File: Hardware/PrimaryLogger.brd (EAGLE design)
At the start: 52.1 x 77.1 mm, 92 parts, among them J1 CONN_42.54_SCREW, J2 CONN_42.54_SCREW, J3 CONN_42.54_SCREW, J4 CONN_42.54_SCREW, J5 CONN_32.54_SCREW, Q1 DMG3404, Q2 DMG3404, U1 MIC2005, U10 TPL5010DDC, U11 MIC842, U12 PCA9617TSSOP8, U13 MCP23008SSOP, U2 MIC2005, U25 SN74AUP3G34DCU, U3 TPL5010DDC, U4 TXS0102DCU, U5 SN74LVC1G3157SC70, U6 TCS3400, U7 SHTC3DFN, U8 MCP23008QFN, U9 MCP7940SOIC

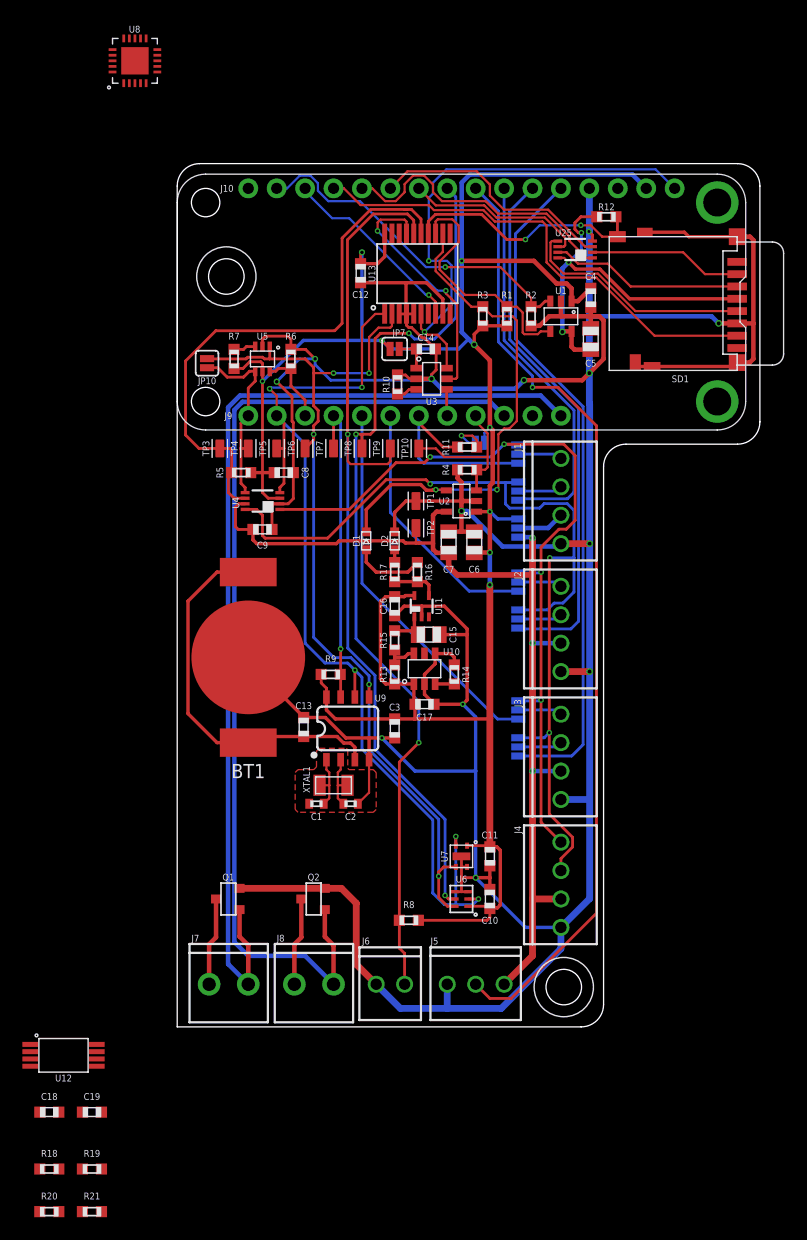
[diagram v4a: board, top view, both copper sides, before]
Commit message: Added Niagara, jumpers, power connector
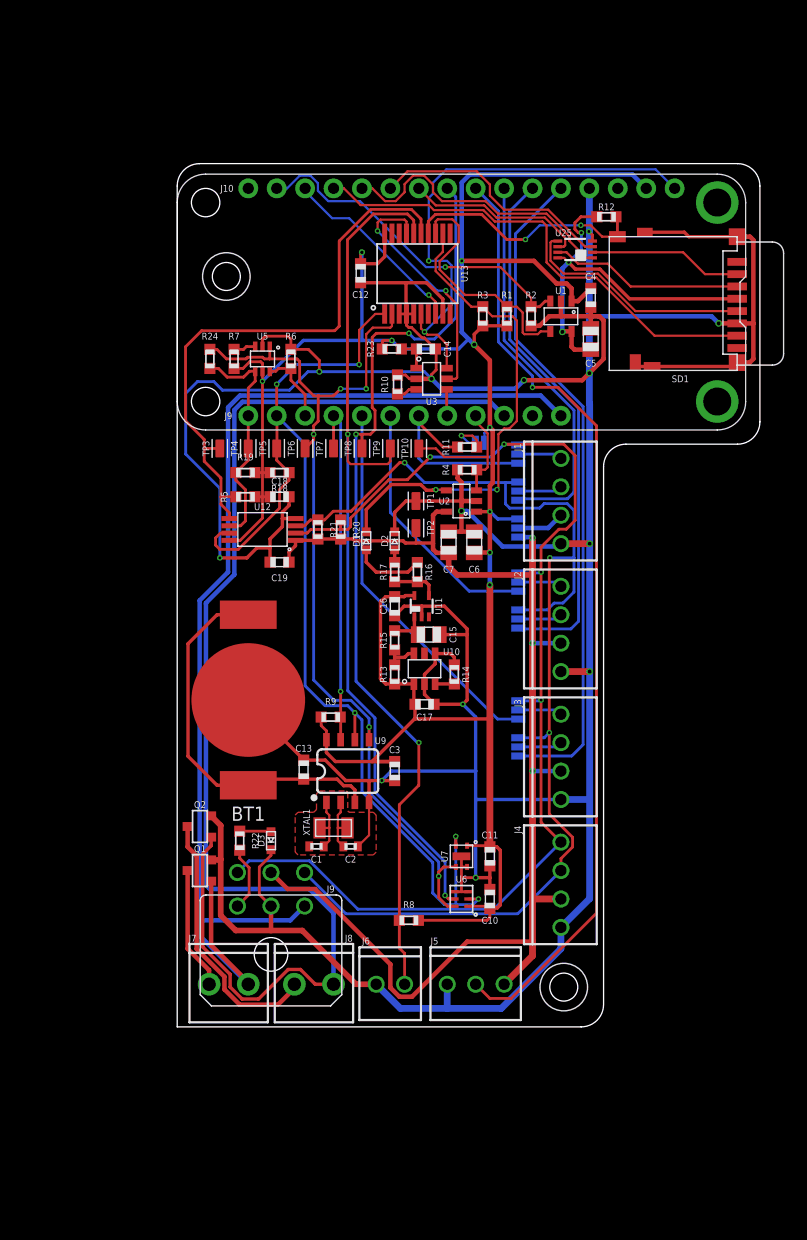
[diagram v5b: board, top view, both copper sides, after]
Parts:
- removed C8, C9: 0.1uF, bschulz_passives:C0603
- removed JP10: JUMPER-SMT_2_NO_SILK, bschulz:SMT-JUMPER_2_NO_SILK
- removed JP7: JUMPER-SMT_2_NC_PASTE_SILK, SparkFun-Jumpers:SMT-JUMPER_2_NC_PASTE_SILK
- removed U4: TXS0102DCU, bschulz:DCU_(R-PDSO-G8)
- removed U8: MCP23008QFN, bschulz:QFN20
- added D3: LEDRED0603, bschulz:LED_0603
- added J9: GEMS_POWER_PLUGINPUT, bschulz:2X3_MICROFIT_RT
- added R22: 1k, bschulz_passives:R0603
- added R23, R24: 0R, bschulz_passives:R0603
- H1, H2: device bschulz:4_40 -> bschulz:2_56
- moved R20 66.3 mm to (14.6, 44.5), turned to 270 degrees
- moved R18 65.5 mm to (9.14, 49.5), turned to 180 degrees
- moved R21 64.2 mm to (12.6, 44.5), turned to 270 degrees
- moved R19 63.7 mm to (6.10, 49.5)
- moved C18 58.7 mm to (9.14, 47.4)
- moved C19 51.9 mm to (9.14, 41.5), turned to 180 degrees
- moved U12 50.2 mm to (7.62, 44.5), turned to 180 degrees
- moved Q2 12.0 mm to (2.03, 17.9)
- moved BT1 3.81 mm to (6.35, 29.2)
- moved C13 3.81 mm to (11.3, 23.0)
- moved C3 3.81 mm to (19.4, 22.9)
- moved U9 3.81 mm to (15.2, 22.9)
- moved C1 3.81 mm to (12.4, 16.1)
- moved C2 3.81 mm to (15.5, 16.1)
- moved R9 3.81 mm to (13.7, 27.7)
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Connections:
- removed net SCL_IN: R18.1
- removed net SCL_OUT: R20.1
- removed net SDA_IN: R19.1
- removed net SDA_OUT: R21.1
- removed net VCC_IN: C18.1, R18.2, R19.2
- removed net VCC_OUT: C19.1, R20.2, R21.2
- new net N$13: J9.3, R22.2
- new net N$14: D3.ANODE, R22.1
- net 3V3: now also C18.1, R18.2, R19.2, R23.2; no longer C8.1, JP7.2, U4.3, U8.18
- net 3V3_EXT: now also C19.1, J9.5, R20.2, R21.2; no longer C9.1, U4.7
- net 3V3_EXT_FAULT: no longer U8.9
- net 3V3_SD_FAULT: no longer U8.10
- net GND: now also D3.CATHODE, J9.2; no longer C8.2, C9.2, U4.2, U8.1, U8.17, U8.2, U8.3, U8.EP
- net I2C_EXT_EN: no longer U4.6, U8.12
- net IO_EXP_INT: no longer U8.7
- net N$6: now also R23.1; no longer JP7.1
- net PAR_INT: no longer U8.13
- net RST: no longer U8.4
- net SCL: now also R18.1; no longer U4.4, U8.19
- net SCL_EXT: now also J9.6, R20.1; no longer U4.1
- net SDA: now also R19.1, R24.1; no longer JP10.2, U4.5
- net SDA_EXT: now also J9.4, R21.1; no longer U4.8
- net SDA_OB: now also R24.2; no longer JP10.1, U8.20
- net SD_CD: no longer U8.11
- net VBAT_FEATHER: now also J9.1
- net WAKE: no longer U8.14
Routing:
- net GND: track 381.7 -> 417.1 mm
- net SCL_EXT: track 71.6 -> 106.0 mm
- net 3V3_EXT: track 87.9 -> 112.0 mm
- net VBUS_FEATHER: track 89.9 -> 113.3 mm
- net SDA_EXT: track 84.8 -> 104.9 mm
- net VSYS-: track 7.88 -> 23.7 mm
- net VBAT_FEATHER: track 90.2 -> 105.8 mm
- net 3V3: track 210.0 -> 221.1 mm
- net SCL: track 91.4 -> 100.0 mm
- net N$13: track 0.00 -> 5.77 mm
- net RTC_INT: track 28.4 -> 32.2 mm
- net SDA: track 17.1 -> 20.6 mm
- net VBAT-: track 7.88 -> 11.0 mm
- net N$14: track 0.00 -> 2.81 mm
- net I2C_EXT_EN: track 49.8 -> 51.9 mm
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
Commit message: Cleanup and gerbers for v0.3A
Cleanup of schematic and layout for v0.3A design
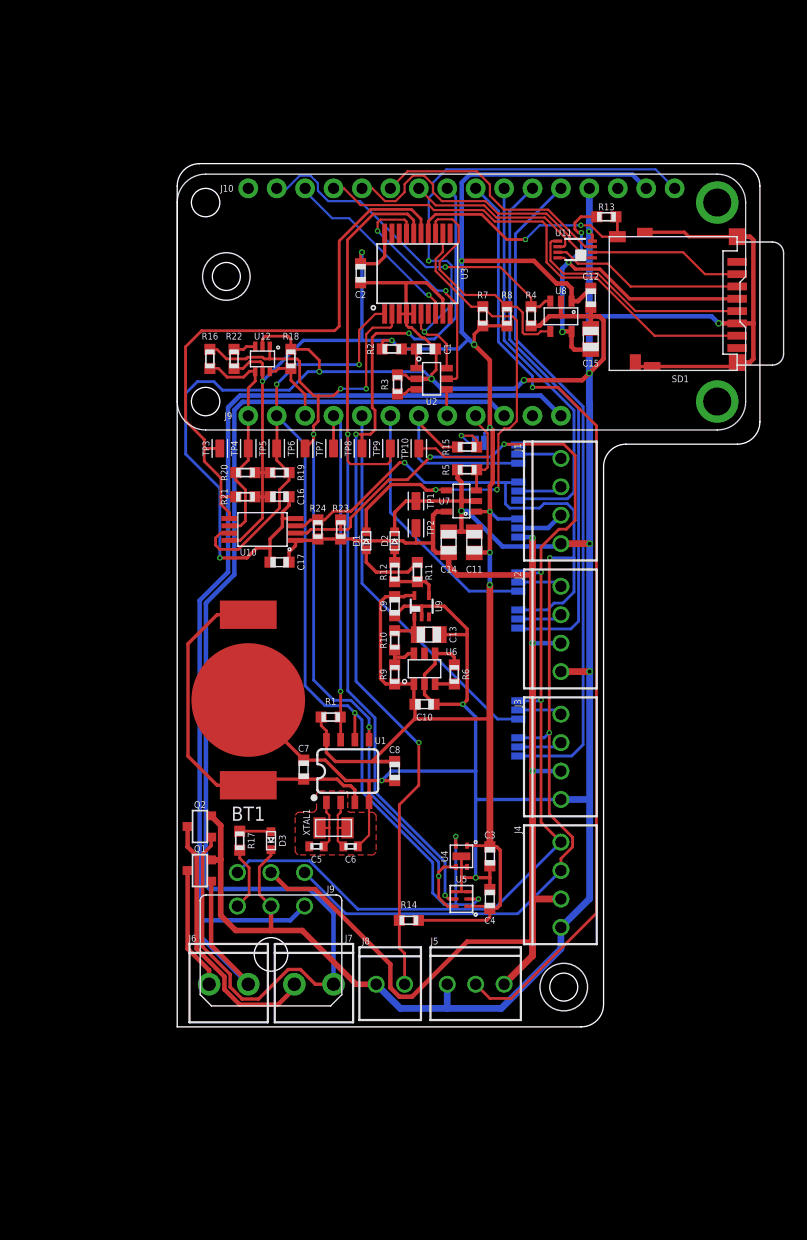
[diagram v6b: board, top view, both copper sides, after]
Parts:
- removed C18, C19: 0.1uF, bschulz_passives:C0603
- removed JP9: JUMPER-SMT_2_NC_PASTE_SILK, bschulz:SMT-JUMPER_2_NC_PASTE_SILK
- removed U13: MCP23008SSOP, bschulz:SSOP20
- removed U25: SN74AUP3G34DCU, bschulz:DCU_(R-PDSO-G8)
- added C8, C9: 0.1uF, bschulz_passives:C0603
- added JP7: JUMPER-SMT_3_1-NC_PASTE_SILK, bschulz:SMT-JUMPER_3_1-NC_PASTE_SILK
- added U4: SHTC3DFN, bschulz:DFN_4_2X2
- added U8: MIC2005, bschulz:SOT23-5
- C1, C2: value 6pF -> 0.1uF; device bschulz_passives:C0402 -> bschulz_passives:C0603
- C10: value 1uF -> 0.1uF
- C11, C13, C14: value 0.1uF -> 10uF; device bschulz_passives:C0603 -> bschulz_passives:C0805
- C12: value 0.1uF -> 1uF
- C5, C6: value 10uF -> 6pF; device bschulz_passives:C0805 -> bschulz_passives:C0402
- C7: value 10uF -> 0.1uF; device bschulz_passives:C0805 -> bschulz_passives:C0603
- J6: device bschulz:1X02_2.54_SCREWTERM_ROUND -> bschulz:SCREWTERMINAL-3.5MM-2_ROUND
- J8: device bschulz:SCREWTERMINAL-3.5MM-2_ROUND -> bschulz:1X02_2.54_SCREWTERM_ROUND
- JP8: value JUMPER-SMT_3_1-NC_PASTE_SILK -> JUMPER-SMT_2_NC_PASTE_SILK; device bschulz:SMT-JUMPER_3_1-NC_PASTE_SILK -> bschulz:SMT-JUMPER_2_NC_PASTE_SILK
- R10, R6, R9: value 100k -> 10k
- R11, R12: value 100k -> 4.7k
- R13, R14, R15: value 10k -> 100k
- R16: value 4.7k -> 0R
- R17: value 4.7k -> 1k
- R18, R21: value (none) -> 100k
- R2: value 100k -> 0R
- R22: value 1k -> 100k
- R23, R24: value 0R -> (none)
- U1: value MIC2005 -> MCP7940SOIC; device bschulz:SOT23-5 -> bschulz:SO08
- U10: value TPL5010DDC -> PCA9617TSSOP8; device bschulz:DDC_R-PDSO-G6 -> bschulz:TTSOP_8
- U11: value MIC842 -> SN74AUP3G34DCU; device bschulz:DCK_R-PDSO-G5 -> bschulz:DCU_(R-PDSO-G8)
- U12: value PCA9617TSSOP8 -> SN74LVC1G3157SC70; device bschulz:TTSOP_8 -> bschulz:DCK_R-PDSO-G6
- U2: value MIC2005 -> TPL5010DDC; device bschulz:SOT23-5 -> bschulz:DDC_R-PDSO-G6
- U3: value TPL5010DDC -> MCP23008SSOP; device bschulz:DDC_R-PDSO-G6 -> bschulz:SSOP20
- U5: value SN74LVC1G3157SC70 -> TCS3400; device bschulz:DCK_R-PDSO-G6 -> bschulz:TCS3400
- U6: value TCS3400 -> TPL5010DDC; device bschulz:TCS3400 -> bschulz:DDC_R-PDSO-G6
- U7: value SHTC3DFN -> MIC2005; device bschulz:DFN_4_2X2 -> bschulz:SOT23-5
- U9: value MCP7940SOIC -> MIC842; device bschulz:SO08 -> bschulz:DCK_R-PDSO-G5
- moved R8 54.7 mm to (29.5, 63.5), turned to 270 degrees
- moved C4 54.5 mm to (27.9, 11.4), turned to 90 degrees
- moved C5 51.5 mm to (12.4, 16.1), turned to 180 degrees
- moved U5 51.4 mm to (25.4, 11.4)
- moved C2 51.2 mm to (16.4, 67.3), turned to 270 degrees
- moved C1 45.5 mm to (22.2, 60.6), turned to 0 degrees
- moved R13 45.1 mm to (38.4, 72.4), turned to 180 degrees
- moved U1 44.9 mm to (15.2, 22.9), turned to 0 degrees
- moved R22 43.1 mm to (5.08, 59.7)
- moved R1 39.1 mm to (13.7, 27.7), turned to 180 degrees
- moved R12 37.0 mm to (19.4, 40.6), turned to 270 degrees
- moved U11 34.7 mm to (35.6, 69.5), turned to 90 degrees
- moved R6 31.8 mm to (24.8, 31.5)
- moved U7 31.8 mm to (25.4, 47.0), turned to 90 degrees
- moved C15 30.1 mm to (37.0, 61.5), turned to 90 degrees
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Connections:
- net 3V3: now also C2.1, C8.1, C9.1, JP5.1, JP8.2, R14.1, R2.2, R20.2, R21.2, R22.2, R8.2, U1.8, U10.8, U12.5, U3.20, U4.1, U5.1, U8.1, U9.5; no longer C17.1, C18.1, C6.1, JP8.1, JP9.2, R13.2, R18.2, R23.2, R3.2, R5.2, R8.1, U1.1, U10.1, U11.5, U12.8, U13.20, U2.1, U5.5, U9.8
- net 3V3_EXT: now also C14.1, C17.1, JP5.3, R23.2, R24.2, U10.1, U7.5; no longer C19.1, C7.1, JP8.3, R20.2, R21.2, U12.1, U2.5
- net 3V3_EXT_EN: now also R5.2, U7.3; no longer R4.2, U2.3
- net 3V3_EXT_FAULT: now also R7.1, U3.12, U7.4; no longer R3.1, U13.12, U2.4
- net 3V3_SD: now also C15.1, R13.2, U11.8, U8.5; no longer C5.1, R12.2, U1.5, U25.8
- net 3V3_SD_EN: now also R4.2, U8.3; no longer R2.2, U1.3
- net 3V3_SD_FAULT: now also R8.1, U3.13, U8.4; no longer R1.1, U1.4, U13.13
- net DATA5: now also JP6.2; no longer JP5.2
- net DATA6: now also JP7.2; no longer JP6.2
- net GND: now also C8.2, C9.2, J8.P2, R18.1, R3.1, R5.1, U1.4, U11.4, U12.2, U3.3, U3.4, U3.5, U3.9, U4.4, U4.EP, U5.3, U5.4, U6.2, U7.2, U8.2, U9.2; no longer C18.2, C19.2, J6.P2, R10.1, R14.1, R2.1, U1.2, U10.2, U11.2, U12.4, U13.3, U13.4, U13.5, U13.9, U25.4, U3.2, U5.2, U6.3, U7.4, U7.EP, U9.4
- net GPIO1D: now also R15.1; no longer R11.1
- net GPIO3A: now also JP7.1; no longer JP6.1
- net GPIO3D: now also JP6.1; no longer JP5.1
- net I2C_EXT_EN: now also R21.1, U10.5, U3.15; no longer R5.1, U12.5, U13.15
- net IO_EXP_INT: now also U3.8; no longer U13.8
- net MOSI: now also U11.1; no longer U25.1
- net MOSI_BUF: now also U11.7; no longer U25.7
- net N$1: now also C5.1, U1.1; no longer C1.1, U9.1
- net N$10: now also R11.2, R12.2, U9.4; no longer R16.2, R17.2, U11.4
- net N$11: now also R11.1; no longer R16.1
- net N$12: now also R12.1; no longer R17.1
- net N$13: now also R17.2; no longer R22.2
- net N$14: now also R17.1; no longer R22.1
- net N$2: now also C6.1, U1.2; no longer C2.1, U9.2
- net N$3: now also R3.2, U2.3; no longer R10.2, U3.3
- net N$4: now also R22.1, U12.3; no longer R7.1, U5.3
- net N$5: now also JP8.1, R15.2; no longer JP9.1, R11.2
- net N$6: now also C1.1, R2.1, U2.1; no longer C14.1, R23.1, U3.1
- net N$7: now also R6.2, U6.3; no longer R14.2, U10.3
- net N$8: now also C13.1, R10.2, U9.1; no longer C15.1, R15.2, U11.1
- net N$9: now also R10.1, R9.1, U6.6; no longer R13.1, R15.1, U10.6
- net PAR_INT: now also U3.16, U5.5; no longer U13.16, U6.5
- net PWR_P1: now also JP5.2; no longer JP8.2
- net RST: now also U2.6; no longer U13.6
- net RTC_INT: now also R1.1, U1.7; no longer R9.1, U9.7
- net SCK: now also U11.3; no longer U25.3
- net SCK_BUF: now also U11.5; no longer U25.5
- net SCL: now also R19.1, U1.6, U10.7, U3.1, U4.2, U5.2; no longer R18.1, U12.7, U13.1, U6.2, U7.2, U9.6
- net SCL_EXT: now also JP6.3, R23.1, U10.2; no longer JP5.3, R20.1, U12.2
- net SDA: now also R16.1, R20.1, U10.6, U12.4; no longer R19.1, R24.1, U12.6, U5.4
- net SDA_CTRL: now also R18.2, U12.6; no longer R6.2, U5.6
- net SDA_EXT: now also JP7.3, R24.1, U10.3; no longer JP6.3, R21.1, U12.3
- net SDA_OB: now also R16.2, U1.5, U12.1, U3.2, U4.3, U5.6; no longer R24.2, U13.2, U5.1, U6.6, U7.3, U9.5
- net SD_CD: now also R13.1, U3.14; no longer R12.1, U13.14
- net SD_CS: now also U11.6; no longer U25.6
- net SD_CS_BUF: now also U11.2; no longer U25.2
- net TIP: now also J8.P1, R14.2; no longer J6.P1, R8.2
- net VBAT: now also C7.1, U1.3; no longer C13.1, U9.3
- net VBAT-: now also J6.2; no longer J7.2
- net VBAT_FEATHER: now also J6.1; no longer J7.1
- net VBUS_FEATHER: now also J7.1; no longer J8.1
- net VSYS-: now also J7.2; no longer J8.2
- net WAKE: now also U2.5, U3.17; no longer U13.17, U3.5
- net WD_HOLD: now also U2.4; no longer U3.4
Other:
- board text added: "Project Hyena v0.3A Bobby Schulz UMN/GEMS"
- board text removed: "Project Hyena v0.2 Bobby Schulz UMN/GEMS"

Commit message: Updated part values for BoM generation
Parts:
- D1: value LED0603 -> LEDRED0603
- D2: value LED0603 -> LEDGREEN0603
- R14: value 100k -> 10k
- R19, R20, R23, R24: value (none) -> 4.7k
- U1: value MCP7940SOIC -> MCP79412SOIC
- U9: value MIC842 -> MIC842L

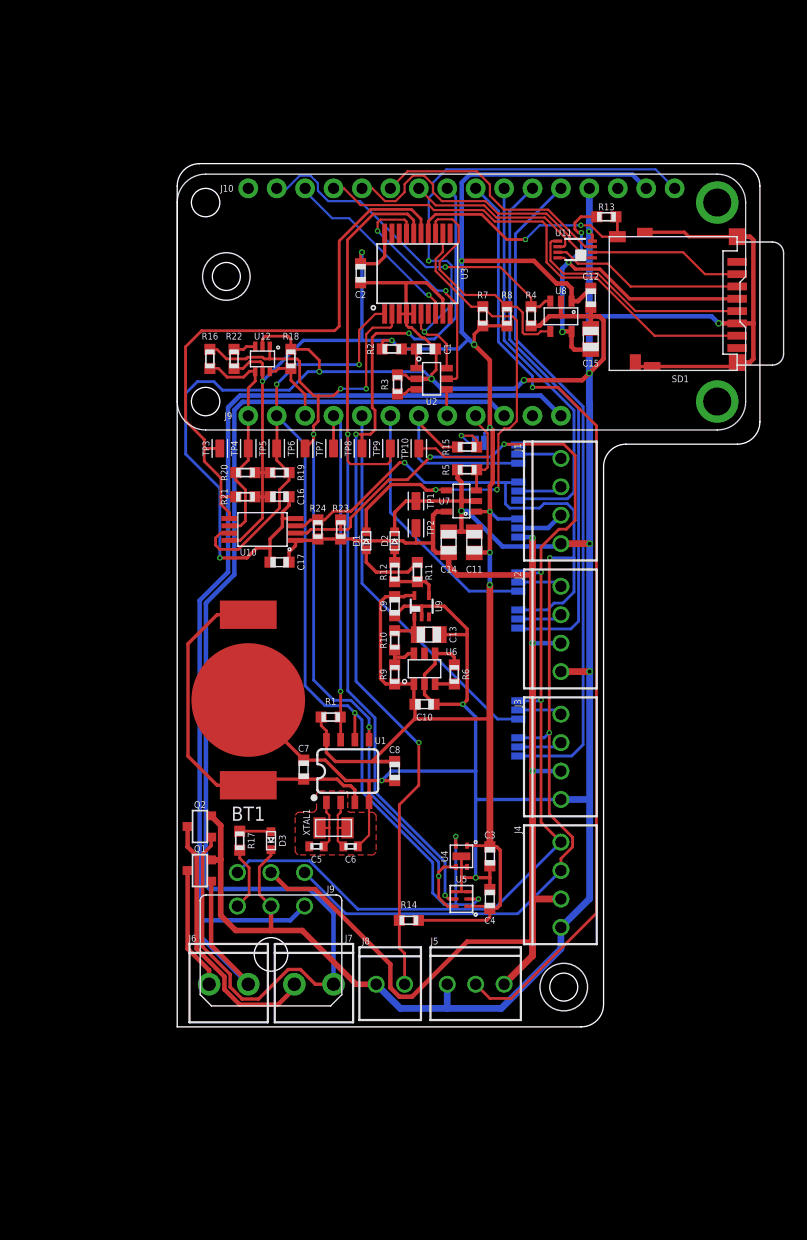
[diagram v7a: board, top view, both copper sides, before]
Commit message: Minor updates v0.4A sent to fab
Fixed layout issues and changed power topology for I2C buffer
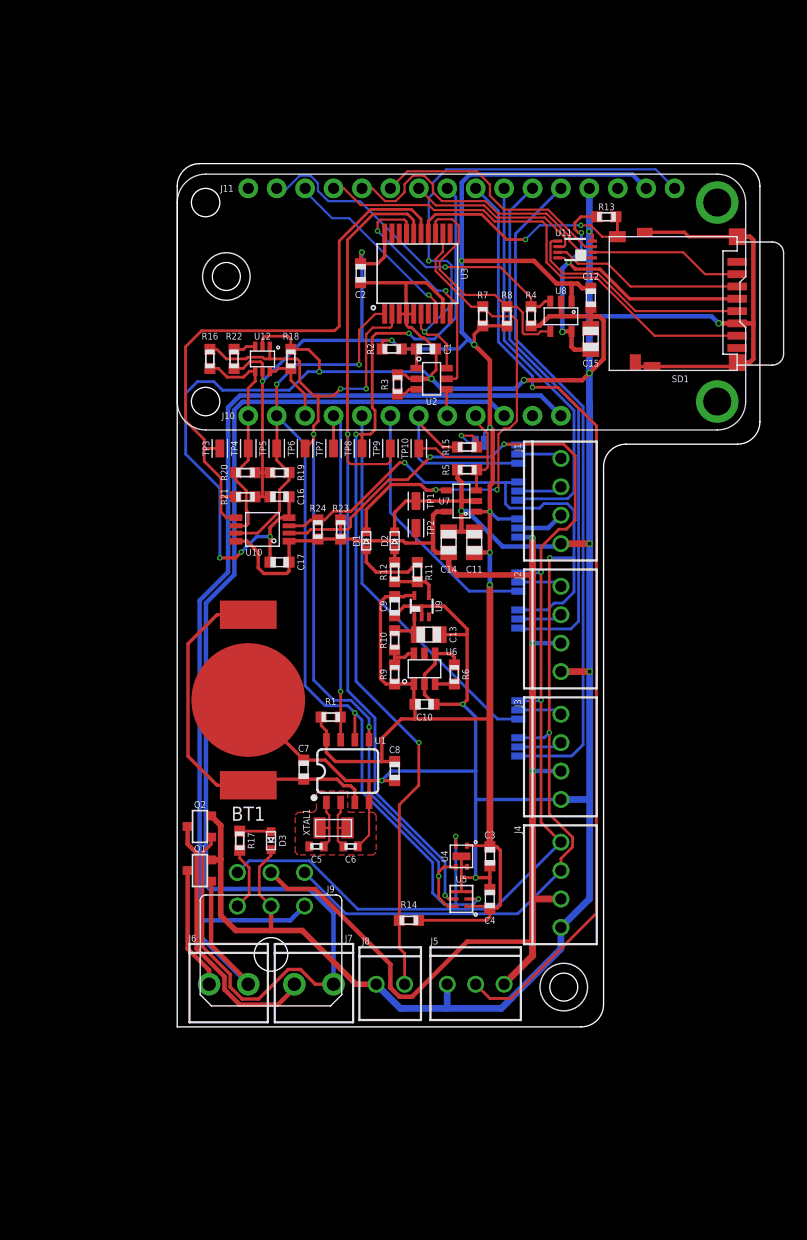
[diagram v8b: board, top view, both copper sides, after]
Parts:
- R16: value 0R -> DNP
- U10: value PCA9617TSSOP8 -> PCA9617; device bschulz:TTSOP_8 -> bschulz:TSSOP_8
- turned U10 to 90 degrees
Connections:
- net 3V3: no longer U10.8
- net 3V3_EXT: now also U10.8
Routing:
- net 3V3_EXT: track 112.0 -> 120.0 mm
- net 3V3: track 221.1 -> 213.6 mm
- net SCL: track 100.0 -> 95.5 mm
- net GND: track 417.1 -> 416.0 mm, vias 13 -> 15
- net I2C_EXT_EN: track 51.9 -> 52.6 mm
- net SDA_EXT: track 104.9 -> 105.5 mm
- net SCL_EXT: track 106.0 -> 106.5 mm
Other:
- board text added: "J11"
- board text added: "Project Hyena v0.4A Bobby Schulz UMN/GEMS"
- board text removed: "J9"
- board text removed: "Project Hyena v0.3A Bobby Schulz UMN/GEMS"
